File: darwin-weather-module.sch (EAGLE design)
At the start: 14 parts, among them U1 P82B715SOIC

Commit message: Schematic Cleanup
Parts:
- removed U$1: 2X6-HEADERS, Conservify:2X6-HEADERS
- removed U$2: ATSAMD09, Conservify:ATSAMD09
- removed U$3: M24C02-WMN6TP, Conservify:M24C02-WMN6TP
- removed U$5: 95501-6889VERT, Conservify:95501-6889VERT
- added J1: 2X6-HEADERS, Conservify:2X6-HEADERS
- added J2: 95501-6889VERT, Conservify:95501-6889VERT
- added U2: ATSAMD09, Conservify:ATSAMD09
- added U3: M24C02-WMN6TP, Conservify:M24C02-WMN6TP
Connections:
- net 3V3: now also U2.VDD, U3.VCC; no longer U$2.VDD, U$3.VCC
- net ENABLE: now also J1.PIN10; no longer U$1.PIN10
- net G1: now also J1.PIN11; no longer U$1.PIN11
- net G2: now also J1.PIN12; no longer U$1.PIN12
- net GND: now also J1.PIN8, J2.P1, J2.P2, J2.P3, U2.GND, U3.E0, U3.E1, U3.E2, U3.VSS; no longer U$1.PIN8, U$2.GND, U$3.E0, U$3.E1, U$3.E2, U$3.VSS, U$5.P1, U$5.P2, U$5.P3
- net IN3V3: now also J1.PIN9; no longer U$1.PIN9
- net LCL: now also J2.P7; no longer U$5.P7
- net LDA: now also J2.P8; no longer U$5.P8
- net MISO: now also J1.PIN4; no longer U$1.PIN4
- net MOSI: now also J1.PIN5; no longer U$1.PIN5
- net NC: now also J1.PIN1; no longer U$1.PIN1
- net RESET: now also U2.PA28/!RESET; no longer U$2.PA28/!RESET
- net SCK: now also J1.PIN6; no longer U$1.PIN6
- net SCL: now also J1.PIN2, U2.PA15, U3.SCL; no longer U$1.PIN2, U$2.PA15, U$3.SCL
- net SDA: now also J1.PIN3, U2.PA14, U3.SDA; no longer U$1.PIN3, U$2.PA14, U$3.SDA
- net SENSE-SCL: now also U2.PA23; no longer U$2.PA23
- net SENSE-SDA: now also U2.PA22; no longer U$2.PA22
- net SWCLK: now also U2.PA30; no longer U$2.PA30
- net SWDIO: now also U2.PA31; no longer U$2.PA31
- net UNREG: now also J1.PIN7, J2.P4, J2.P5, J2.P6; no longer U$1.PIN7, U$5.P4, U$5.P5, U$5.P6
- net WC: now also U2.PA16, U3.!WC; no longer U$2.PA16, U$3.!WC
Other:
- note added: "CONNECTORS"
- note added: "EEPROM"
- note added: "I2C EXTENDER"
- note added: "MCU"
- note added: "POWER"
- moved on the sheet: C1, C2, C3, C7, C8, C9, R1, U1, X1

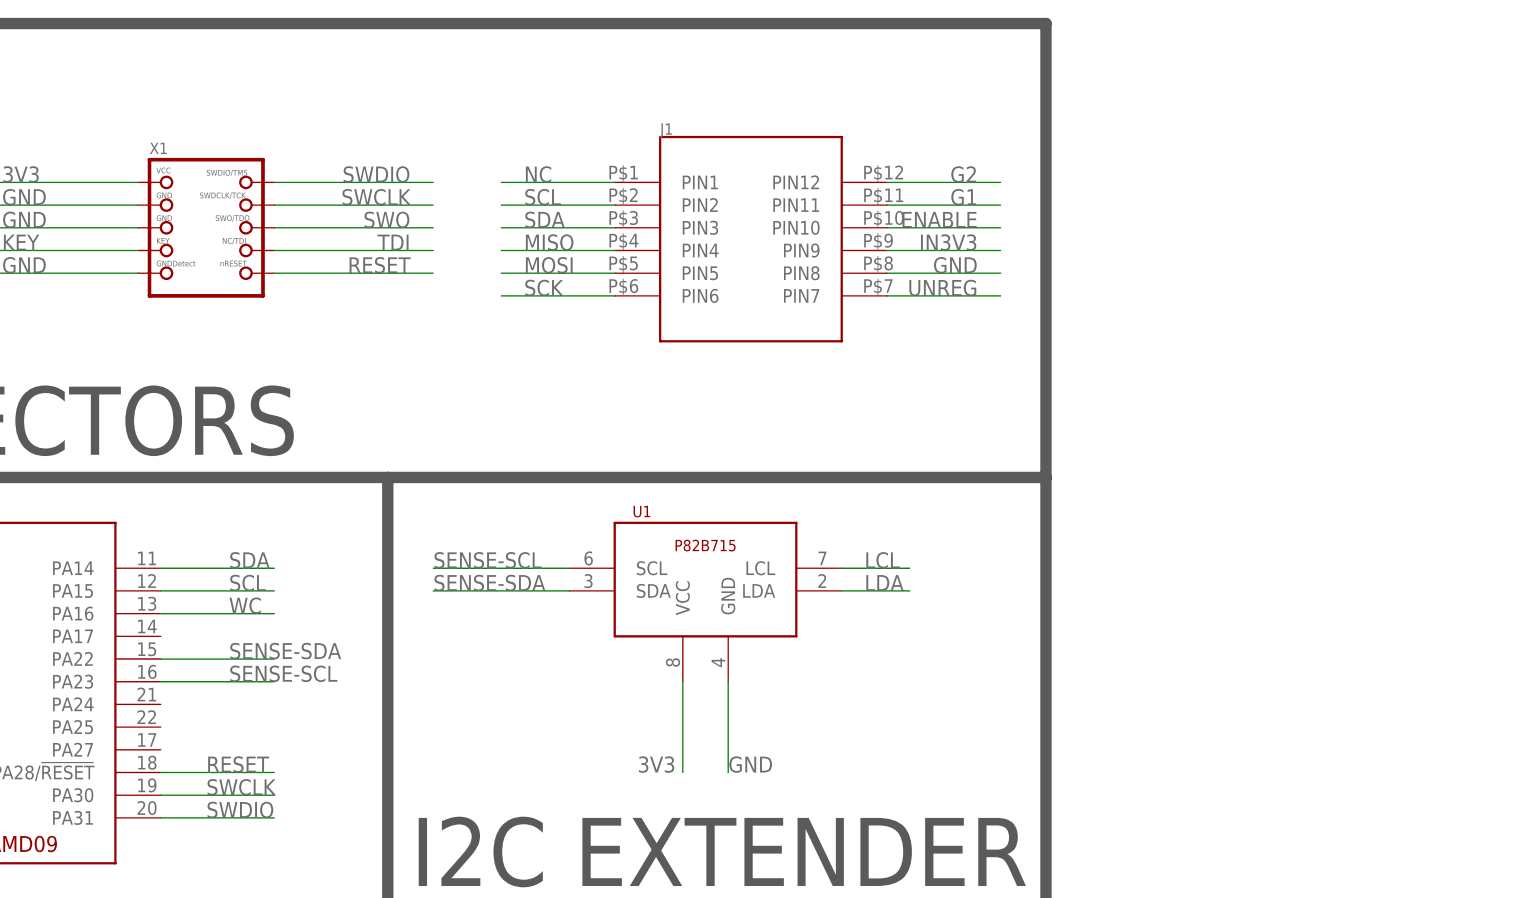
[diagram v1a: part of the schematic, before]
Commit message: Added I2C Pullups and GPIO connection to backplane. Removed deprecated module mounting hole.
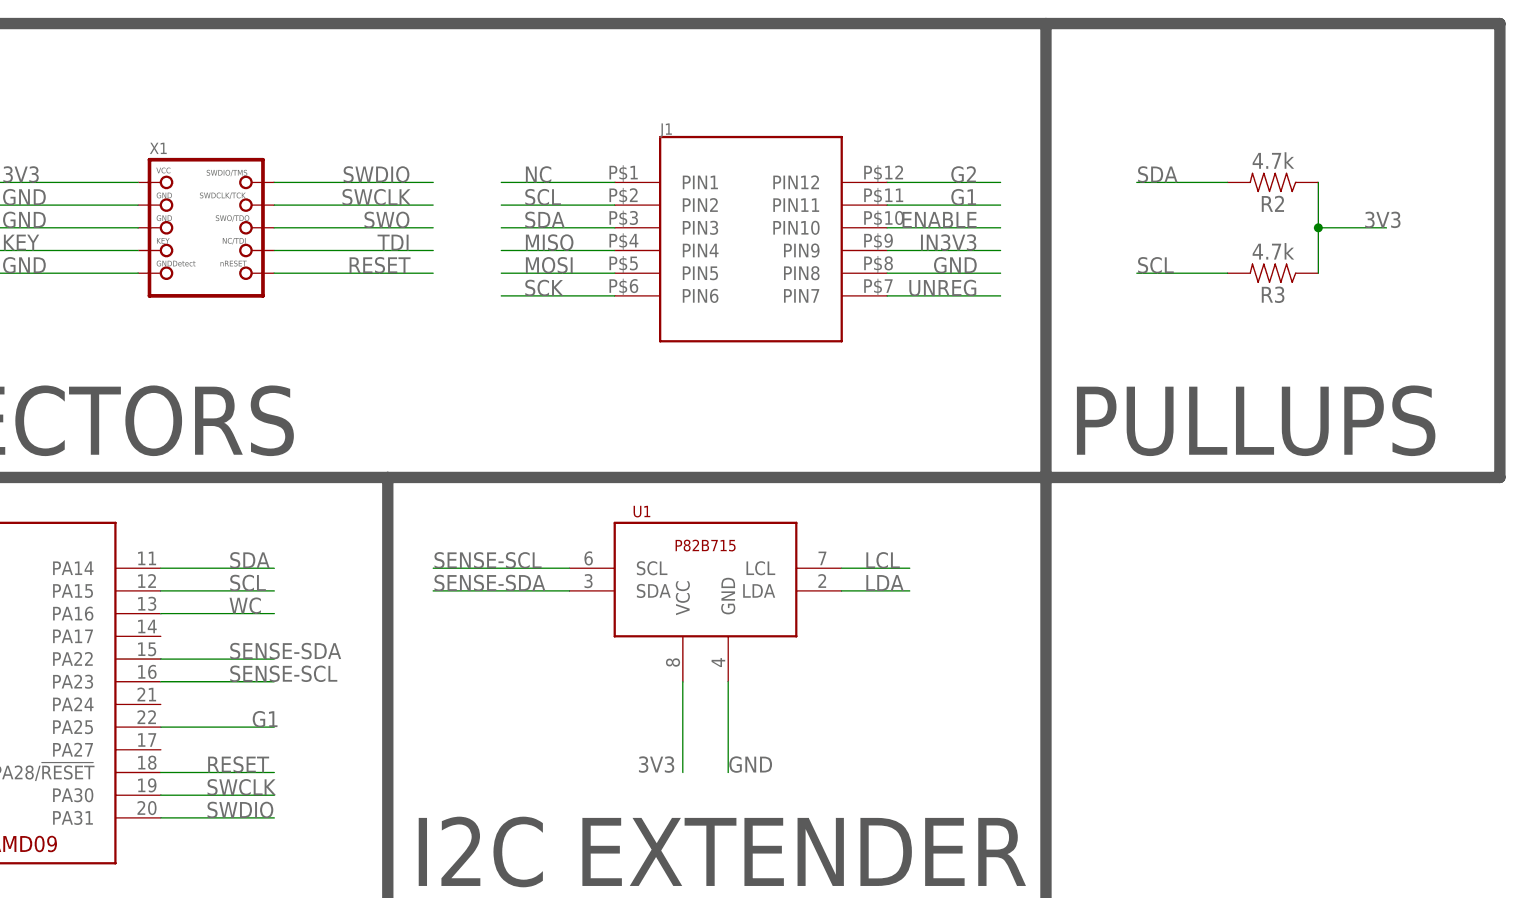
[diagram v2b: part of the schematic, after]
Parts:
- added R2, R3: 4.7k, SparkFun-Resistors:100KOHM-0603-1/10W-1%
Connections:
- net 3V3: now also R2.1, R3.1
- net G1: now also U2.PA25
- net SCL: now also R3.2
- net SDA: now also R2.2
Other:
- note added: "PULLUPS"
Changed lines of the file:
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@@
 <part name="C2" library="rcl" library_urn="urn:adsk.eagle:library:334" deviceset="C-US" device="C0603K" package3d_urn="urn:adsk.eagle:package:23680/2" value=".1uf"/>
 <part name="C3" library="rcl" library_urn="urn:adsk.eagle:library:334" deviceset="C-US" device="C0603K" package3d_urn="urn:adsk.eagle:package:23680/2" value=".1uf"/>
+<part name="R2" library="SparkFun-Resistors" library_urn="urn:adsk.eagle:library:532" deviceset="100KOHM" device="-0603-1/10W-1%" package3d_urn="urn:adsk.eagle:package:39650/1" value="4.7k"/>
+<part name="R3" library="SparkFun-Resistors" library_urn="urn:adsk.eagle:library:532" deviceset="100KOHM" device="-0603-1/10W-1%" package3d_urn="urn:adsk.eagle:package:39650/1" value="4.7k"/>
 </parts>
 <sheets>
@@
 <wire x1="40.64" y1="-43.18" x2="132.08" y2="-43.18" width="1.27" layer="97"/>
 <wire x1="132.08" y1="-43.18" x2="132.08" y2="15.24" width="1.27" layer="97"/>
+<wire x1="193.04" y1="114.3" x2="243.84" y2="114.3" width="1.27" layer="97"/>
+<wire x1="243.84" y1="114.3" x2="243.84" y2="63.5" width="1.27" layer="97"/>
+<wire x1="243.84" y1="63.5" x2="193.04" y2="63.5" width="1.27" layer="97"/>
+<text x="195.58" y="66.04" size="7.62" layer="97">PULLUPS</text>
 </plain>
 <instances>
@@
 <attribute name="NAME" x="92.456" y="-19.685" size="1.778" layer="95"/>
 <attribute name="VALUE" x="92.456" y="-24.511" size="1.778" layer="96"/>
+</instance>
+<instance part="R2" gate="G$1" x="218.44" y="96.52" smashed="yes" rot="R180">
+<attribute name="NAME" x="218.44" y="94.996" size="1.778" layer="95" font="vector" rot="R180" align="bottom-center"/>
+<attribute name="VALUE" x="218.44" y="98.044" size="1.778" layer="96" font="vector" rot="R180" align="top-center"/>
+</instance>
+<instance part="R3" gate="G$1" x="218.44" y="86.36" smashed="yes" rot="R180">
+<attribute name="NAME" x="218.44" y="84.836" size="1.778" layer="95" font="vector" rot="R180" align="bottom-center"/>
+<attribute name="VALUE" x="218.44" y="87.884" size="1.778" layer="96" font="vector" rot="R180" align="top-center"/>
 </instance>
 </instances>
@@
 <label x="83.82" y="-17.78" size="1.778" layer="95"/>
 </segment>
+<segment>
+<pinref part="R3" gate="G$1" pin="1"/>
+<pinref part="R2" gate="G$1" pin="1"/>
+<wire x1="223.52" y1="86.36" x2="223.52" y2="91.44" width="0.1524" layer="91"/>
+<wire x1="223.52" y1="91.44" x2="223.52" y2="96.52" width="0.1524" layer="91"/>
+<wire x1="223.52" y1="91.44" x2="231.14" y2="91.44" width="0.1524" layer="91"/>
+<junction x="223.52" y="91.44"/>
+<label x="228.6" y="91.44" size="1.778" layer="95"/>
+</segment>
 </net>
 <net name="N$6" class="0">
@@
 <label x="134.62" y="91.44" size="1.778" layer="95"/>
 </segment>
+<segment>
+<pinref part="R2" gate="G$1" pin="2"/>
+<wire x1="213.36" y1="96.52" x2="203.2" y2="96.52" width="0.1524" layer="91"/>
+<label x="203.2" y="96.52" size="1.778" layer="95"/>
+</segment>
 </net>
 <net name="SCL" class="0">
@@
 <wire x1="144.78" y1="93.98" x2="132.08" y2="93.98" width="0.1524" layer="91"/>
 <label x="134.62" y="93.98" size="1.778" layer="95"/>
+</segment>
+<segment>
+<pinref part="R3" gate="G$1" pin="2"/>
+<wire x1="213.36" y1="86.36" x2="203.2" y2="86.36" width="0.1524" layer="91"/>
+<label x="203.2" y="86.36" size="1.778" layer="95"/>
 </segment>
 </net>
@@
 <label x="185.42" y="93.98" size="1.778" layer="95" align="bottom-right"/>
 </segment>
-</net>
+<segment>
+<pinref part="U2" gate="G$1" pin="PA25"/>
+<wire x1="93.98" y1="35.56" x2="106.68" y2="35.56" width="0.1524" layer="91"/>
+<label x="104.14" y="35.56" size="1.778" layer="95"/>
+</segment>
+</net>

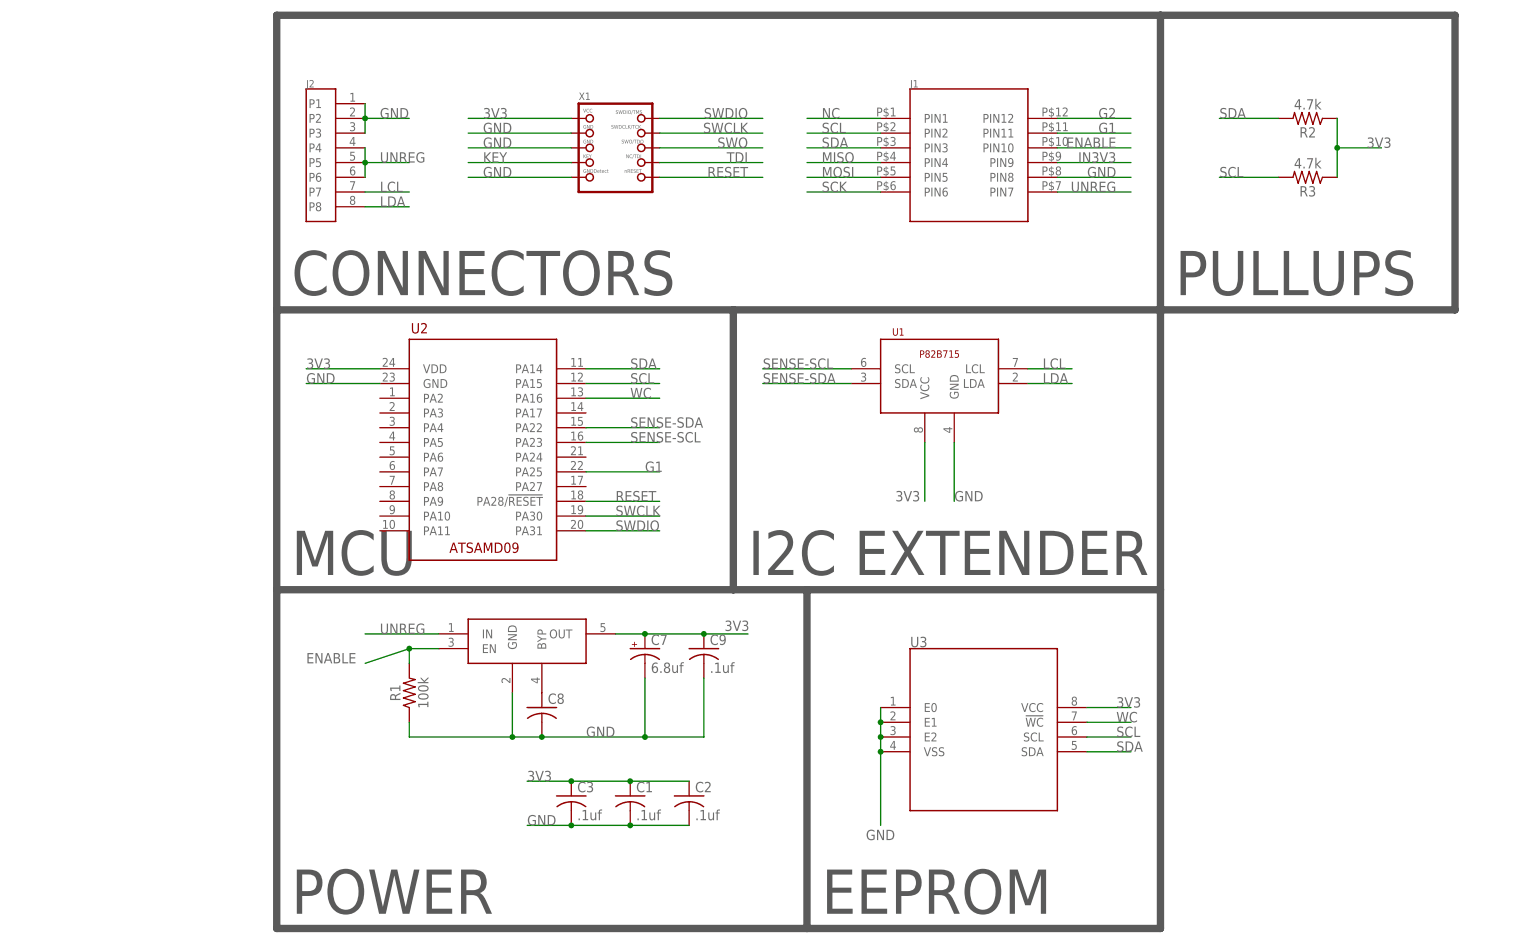
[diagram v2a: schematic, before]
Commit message: Changed range extender to PCA9615
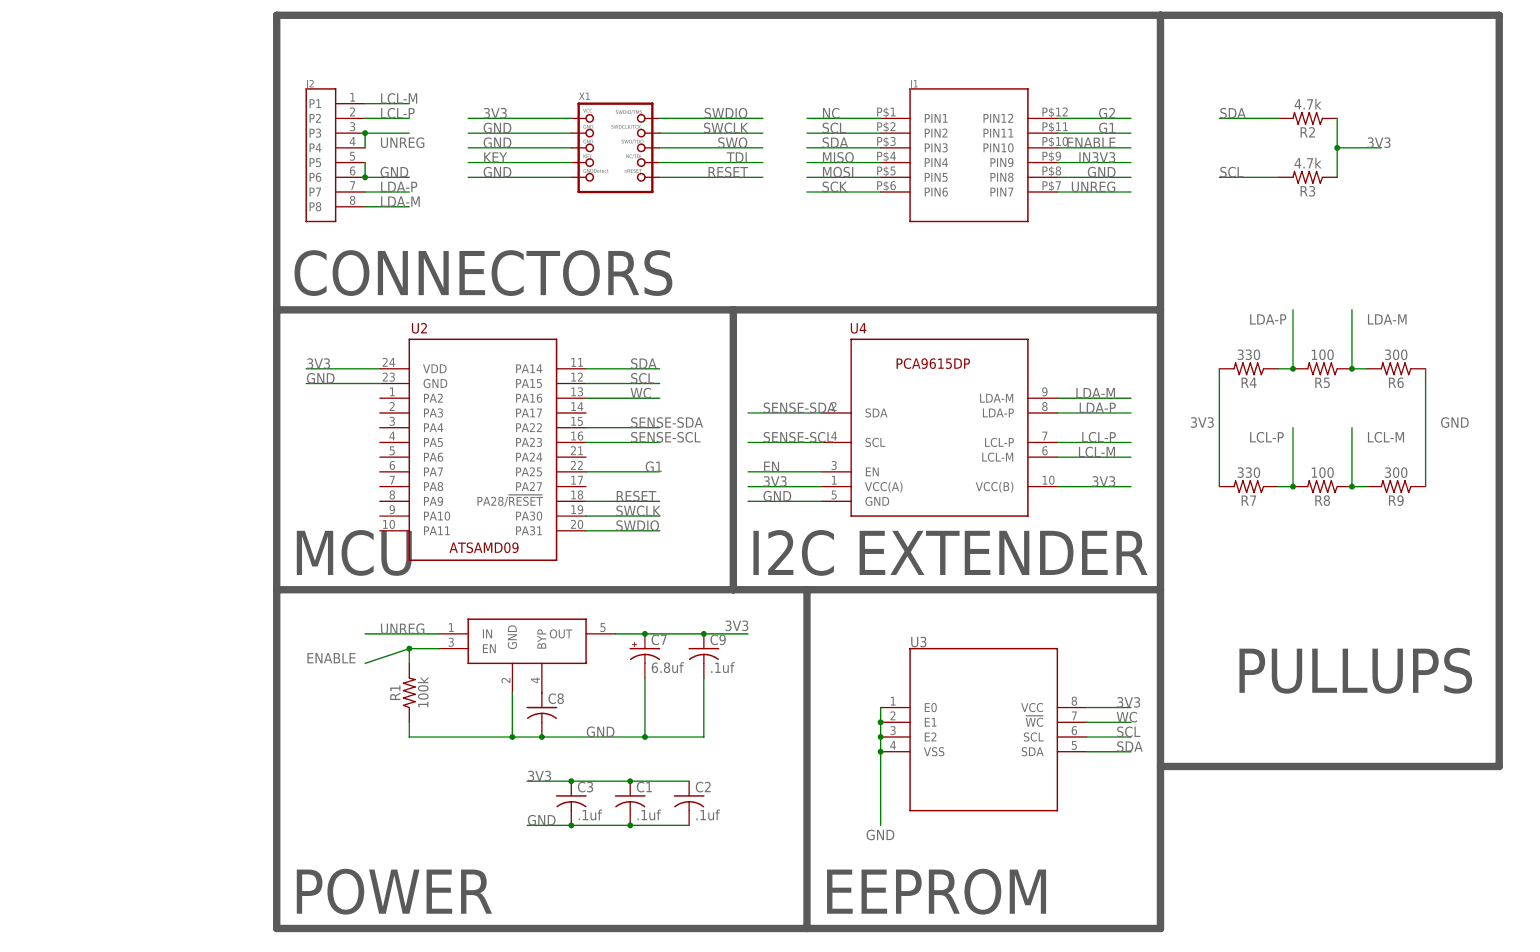
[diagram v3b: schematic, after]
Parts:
- removed U1: P82B715SOIC, Conservify:P82B715SOIC
- added R4, R7: 330, SparkFun-Resistors:100KOHM-0603-1/10W-1%
- added R5, R8: 100, SparkFun-Resistors:100KOHM-0603-1/10W-1%
- added R6, R9: 300, SparkFun-Resistors:100KOHM-0603-1/10W-1%
- added U4: PCA9615, Conservify:PCA9615
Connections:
- removed net LCL: J2.P7, U1.LCL
- removed net LDA: J2.P8, U1.LDA
- new net EN: U4.EN
- new net LCL-M: J2.P1, R8.1, R9.2, U4.LCL-M
- new net LCL-P: J2.P2, R7.1, R8.2, U4.LCL-P
- new net LDA-M: J2.P8, R5.1, R6.2, U4.LDA-M
- new net LDA-P: J2.P7, R4.1, R5.2, U4.LDA-P
- net 3V3: now also R4.2, R7.2, U4.VCC(A), U4.VCC(B); no longer U1.VCC
- net GND: now also J2.P5, J2.P6, R6.1, R9.1, U4.GND; no longer J2.P1, J2.P2, J2.P3, U1.GND
- net SENSE-SCL: now also U4.SCL; no longer U1.SCL
- net SENSE-SDA: now also U4.SDA; no longer U1.SDA
- net UNREG: now also J2.P3; no longer J2.P5, J2.P6
